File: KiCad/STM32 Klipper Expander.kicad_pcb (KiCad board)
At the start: 2 copper layers, 44.4 x 44.5 mm, 28 parts, among them J1 Conn_01x04, J2 USB_B_Micro, J3 Conn_02x05, J4 Conn_01x03, J5 Screw_Terminal_01x08, Q1 IRLML6344TRPBF, Q2 IRLML6344TRPBF, Q3 IRLML6344TRPBF, Q4 IRLML6344TRPBF, SW1 SW_SPST, SW2 SW_SPST, U1 STM32F042F6Px, U2 AP2127K-3.3

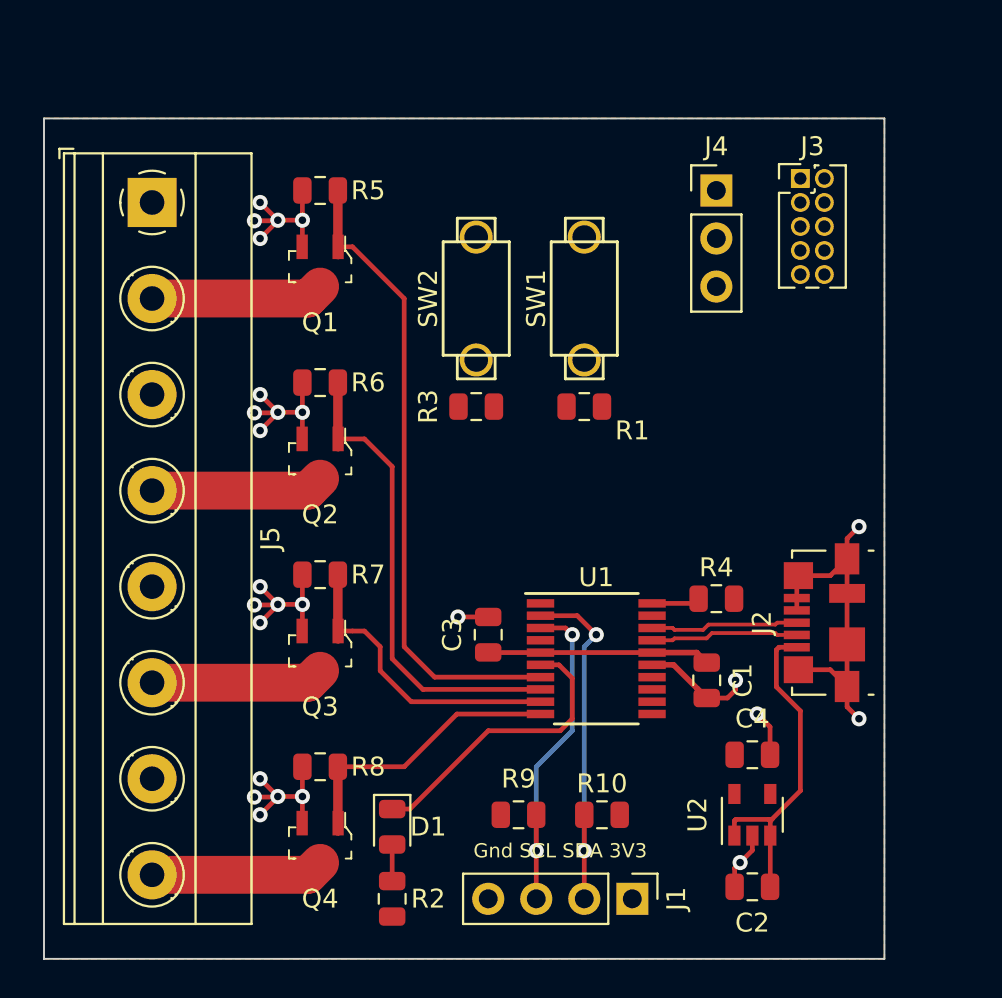
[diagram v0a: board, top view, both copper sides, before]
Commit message: V1 Finalization
Added all components, silkscreen on bottom with pin names and newer sot-23 mosfets.
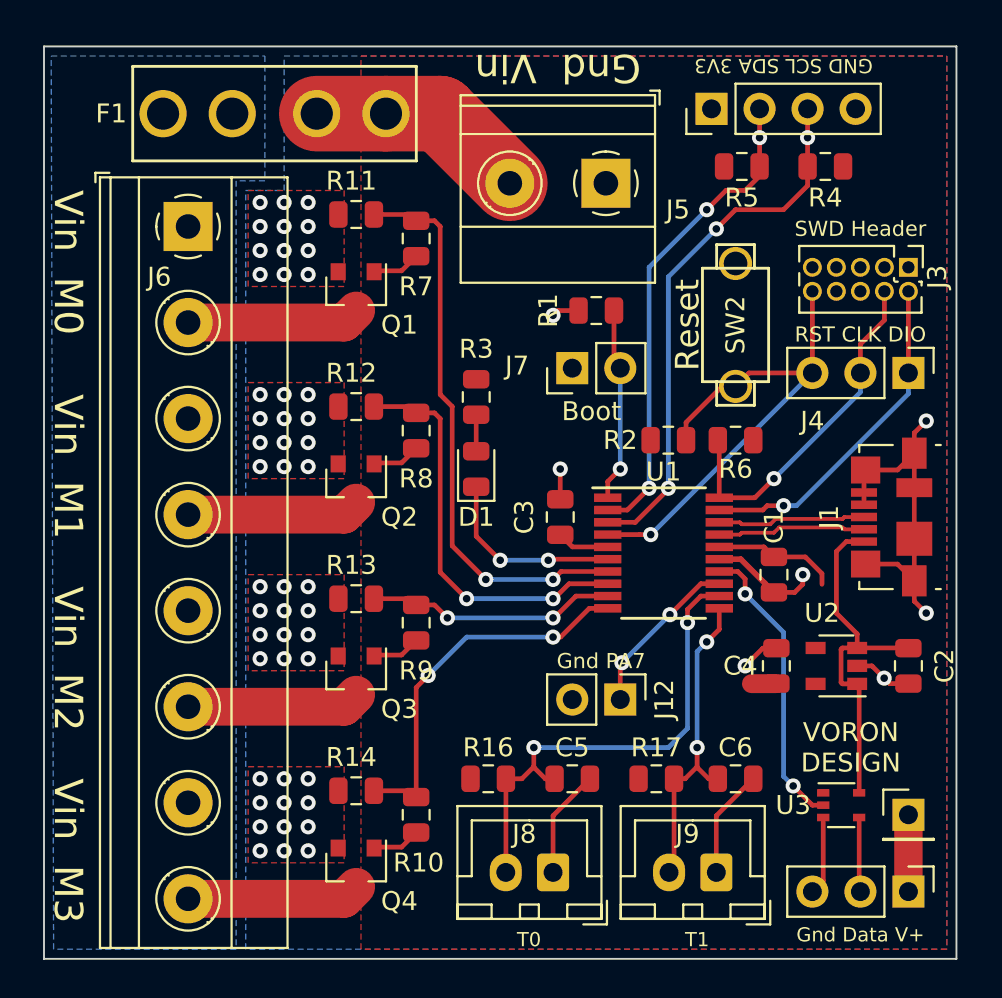
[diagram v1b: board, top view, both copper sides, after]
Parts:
- removed the J1 at (131.1, 96.8)
- removed SW1: SW_SPST, TRA_KiCad_Footprints:2PinTactileButton
- added C5: 10uF, Capacitor_SMD:C_0805_2012Metric, F.Cu at (127.9, 90.5)
- added C6: 10uF, Capacitor_SMD:C_0805_2012Metric, F.Cu at (136.6, 90.5)
- added F1: Fuse, TRA_KiCad_Footprints:3544-2_FuseHolder, F.Cu at (112.2, 55.3)
- added J10: Conn_01x01, Connector_PinHeader_2.54mm:PinHeader_1x01_P2.54mm_Vertical, F.Cu at (145.7, 92.4)
- added J11: Conn_01x03, Connector_PinHeader_2.54mm:PinHeader_1x03_P2.54mm_Vertical, F.Cu at (145.7, 96.4)
- added J12: Conn_01x02, Connector_PinHeader_2.54mm:PinHeader_1x02_P2.54mm_Vertical, F.Cu at (130.5, 86.3)
- added J2: Conn_01x04, Connector_PinHeader_2.54mm:PinHeader_1x04_P2.54mm_Vertical, F.Cu at (135.3, 55.0)
- added J6: Screw_Terminal_01x08, TRA_KiCad_Footprints:TerminalBlock_Phoenix_MKDS-1,5-8-5.08_1x08_P5.08mm_Horizontal, F.Cu at (107.6, 61.3)
- added J7: Conn_01x02, Connector_PinHeader_2.54mm:PinHeader_1x02_P2.54mm_Vertical, F.Cu at (127.9, 68.8)
- added J8: Conn_01x02, Connector_JST:JST_XH_B02B-XH-A_1x02_P2.50mm_Vertical, F.Cu at (126.9, 95.4)
- added J9: Conn_01x02, Connector_JST:JST_XH_B02B-XH-A_1x02_P2.50mm_Vertical, F.Cu at (135.6, 95.4)
- added R11: 10K, Resistor_SMD:R_0805_2012Metric, F.Cu at (116.5, 60.6)
- added R12: 10K, Resistor_SMD:R_0805_2012Metric, F.Cu at (116.5, 70.8)
- added R13: 10K, Resistor_SMD:R_0805_2012Metric, F.Cu at (116.5, 81.0)
- added R14: 10K, Resistor_SMD:R_0805_2012Metric, F.Cu at (116.5, 91.1)
- added R16: 10K, Resistor_SMD:R_0805_2012Metric, F.Cu at (123.5, 90.5)
- added R17: 10K, Resistor_SMD:R_0805_2012Metric, F.Cu at (132.4, 90.5)
- added U3: 74LVC1G17, Package_TO_SOT_SMD:SOT-353_SC-70-5, F.Cu at (142.2, 91.9)
- J5: value Screw_Terminal_01x08 -> Vin; footprint TerminalBlock_Phoenix:TerminalBlock_Phoenix_MKDS-1,5-8-5.08_1x08_P5.08mm_Horizontal -> TRA_KiCad_Footprints:1x02_ScrewTerminal_Phoenix
- Q1, Q2, Q3, Q4: footprint digikey-footprints:SOT-23-3 -> Package_TO_SOT_SMD:SOT-23
- R10, R9: value 4.7K -> 100
- R2: value 1K -> 10K
- R3: value 10K -> 1K
- R4, R5: value 10K -> 4.7K
- R7, R8: value 10K -> 100
- moved R2 28.3 mm to (133.0, 72.6), turned to 0 degrees
- moved J5 24.0 mm to (129.7, 59.0), turned to 180 degrees
- moved R4 23.6 mm to (141.3, 58.1)
- moved R5 22.3 mm to (136.9, 58.1), turned to 180 degrees
- moved R6 22.2 mm to (136.6, 72.6)
- moved D1 19.4 mm to (122.9, 74.1), turned to 90 degrees
- moved R7 18.5 mm to (119.7, 61.9), turned to 270 degrees
- moved R8 18.5 mm to (119.7, 72.1), turned to 270 degrees
- moved C2 14.3 mm to (145.7, 84.5), turned to 90 degrees
- moved J4 14.0 mm to (145.7, 69.0), turned to 270 degrees
- moved SW2 13.8 mm to (136.6, 66.5)
- moved R9 11.5 mm to (119.7, 82.2), turned to 270 degrees
- moved R10 9.83 mm to (119.7, 92.4), turned to 270 degrees
- moved U2 9.04 mm to (141.9, 84.5), turned to 180 degrees
- moved J3 7.40 mm to (145.7, 63.4), turned to 270 degrees
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- renumbered J2 to J1
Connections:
- net /VBUS renamed VCC
- J5 pad 2: /Mosfet0 -> Net-(F1-Pad2)
- Q1 pad 1: PWM0 -> Net-(Q1-Pad1)
- Q2 pad 1: PWM1 -> Net-(Q2-Pad1)
- Q3 pad 1: PWM2 -> Net-(Q3-Pad1)
- Q4 pad 1: PWM3 -> Net-(Q4-Pad1)
- R10 pad 1: /SDA -> PWM3
- R10 pad 2: +3V3 -> Net-(Q4-Pad1)
- R2 pad 1: Net-(D1-Pad2) -> +3V3
- R2 pad 2: +3V3 -> /~RESET
- R3 pad 1: +3V3 -> Net-(D1-Pad2)
- R3 pad 2: /~RESET -> +3V3
- R4 pad 1: /SWDCLK -> /SCL
- R5 pad 1: GND -> /SDA
- R5 pad 2: PWM0 -> +3V3
- R6 pad 1: GND -> /SWDCLK
- R6 pad 2: PWM1 -> +3V3
- R7 pad 1: GND -> PWM0
- R7 pad 2: PWM2 -> Net-(Q1-Pad1)
- R8 pad 1: GND -> PWM1
- R8 pad 2: PWM3 -> Net-(Q2-Pad1)
- R9 pad 1: /SCL -> PWM2
- R9 pad 2: +3V3 -> Net-(Q3-Pad1)
- U1 pad 11: (no net) -> T1
- U1 pad 12: (no net) -> T0
- U1 pad 13: (no net) -> GPIO
- U1 pad 14: (no net) -> Neopixel
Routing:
- net /~RESET: track 0.00 -> 27.4 mm, vias 0 -> 1
- net T0: track 0.00 -> 26.2 mm, vias 0 -> 2
- net /SWDIO: track 0.00 -> 18.0 mm, vias 0 -> 1
- net T1: track 0.00 -> 16.8 mm, vias 0 -> 2
- net /SWDCLK: track 2.57 -> 18.2 mm, vias 0 -> 1
- net Neopixel: track 0.00 -> 15.5 mm, vias 0 -> 2
- net GND: track 63.6 -> 48.1 mm, vias 26 -> 55
- net Net-(F1-Pad2): track 0.00 -> 11.7 mm
- net /BOOT0: track 0.00 -> 10.3 mm, vias 0 -> 1
- net /SCL: track 19.1 -> 29.1 mm, vias 2 -> 3
- net GPIO: track 0.00 -> 8.35 mm, vias 0 -> 2
- net /LED: track 15.6 -> 10.1 mm, vias 0 -> 2
- net /SDA: track 20.1 -> 25.2 mm, vias 2 -> 3
- net PWM3: track 15.3 -> 20.0 mm, vias 0 -> 2
- net PWM0: track 34.3 -> 30.1 mm, vias 0 -> 2
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- added copper zone on B.Cu, net /Vin
- added copper zone on F.Cu, net GND
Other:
- board size 44.4 x 44.5 mm -> 48.3 x 48.3 mm
- board text added: "3V3 PB8"
- board text added: "3V3 PF0 PF1 GND"
- board text added: "Boot"
- board text added: "GND SCL SDA 3V3"
- board text added: "Gnd Data V+"
- board text added: "Gnd PA5"
- board text added: "Gnd PA6"
- board text added: "Gnd PA7"
- board text added: "Gnd Vin"
- board text added: "PA1 Vin"
- board text added: "PA13 PA14 RST"
- board text added: "PA2 Vin"
- board text added: "PA3 Vin"
- board text added: "PA4 Vin"
- board text added: "RST CLK DIO"
- board text added: "Reset"
- board text added: "SWD Header"
- board text added: "T0"
- board text added: "T1"
- board text added: "VORON DESIGN"
- board text added: "Vin"
- board text added: "Vin Gnd"
- board text added: "Vin M0"
- board text added: "Vin M1"
- board text added: "Vin M2"
- board text added: "Vin M3"
- board text added: "Vin PB1 Gnd"
- board text removed: "Gnd SCL SDA 3V3"

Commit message: Update to Gerbers
Updated Gerbers files for production
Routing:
- net GND: track 48.1 -> 47.5 mm
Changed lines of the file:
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@@
     (add_net "Net-(J10-Pad1)")
     (add_net "Net-(J11-Pad2)")
-    (add_net "Net-(J3-Pad6)")
-    (add_net "Net-(J3-Pad7)")
-    (add_net "Net-(J3-Pad8)")
     (add_net "Net-(Q1-Pad1)")
     (add_net "Net-(Q2-Pad1)")
     (add_net "Net-(Q3-Pad1)")
     (add_net "Net-(Q4-Pad1)")
-    (add_net "Net-(U2-Pad4)")
     (add_net PWM0)
     (add_net PWM1)
@@
   (via (at 127.305 74.092) (size 0.8) (drill 0.4) (layers F.Cu B.Cu) (net 2))
   (segment (start 127.305 75.6945) (end 127.305 74.092) (width 0.25) (layer F.Cu) (net 2))
-  (via (at 137.084 84.506) (size 0.8) (drill 0.4) (layers F.Cu B.Cu) (net 2))
-  (segment (start 138.735 83.5685) (end 138.0215 83.5685) (width 0.25) (layer F.Cu) (net 2))
-  (segment (start 138.0215 83.5685) (end 137.084 84.506) (width 0.25) (layer F.Cu) (net 2))
   (segment (start 128.2725 65.71) (end 127.178 65.71) (width 0.25) (layer F.Cu) (net 2))
   (via (at 126.924 65.964) (size 0.8) (drill 0.4) (layers F.Cu B.Cu) (net 2))
@@
   (segment (start 126.924 92.4285) (end 126.924 95.428) (width 0.25) (layer F.Cu) (net 2))
   (segment (start 128.8775 90.475) (end 126.924 92.4285) (width 0.25) (layer F.Cu) (net 2))
+  (via (at 137.338 83.49) (size 0.8) (drill 0.4) (layers F.Cu B.Cu) (net 2))
+  (segment (start 137.4165 83.5685) (end 137.338 83.49) (width 0.25) (layer F.Cu) (net 2))
+  (segment (start 138.735 83.5685) (end 137.4165 83.5685) (width 0.25) (layer F.Cu) (net 2))
   (segment (start 142.154999 85.380999) (end 142.154999 83.631001) (width 0.25) (layer F.Cu) (net 31))
   (segment (start 142.23 85.456) (end 142.154999 85.380999) (width 0.25) (layer F.Cu) (net 31))
